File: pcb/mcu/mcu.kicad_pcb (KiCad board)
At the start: 2 copper layers, 99 x 34 mm, 46 parts, among them J1 Conn_01x02_Male, J3 Conn_01x05_Female, P1 USB_C_6PIN_POWER, SW1 SW_BOOT, SW2 SW_Push_SPDT, U1 SPX3819M5-L-3-3, U2 LTC4054ES5-4.2, U3 LM358, U4 ESP-12S, U6 SGM3002_XMS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

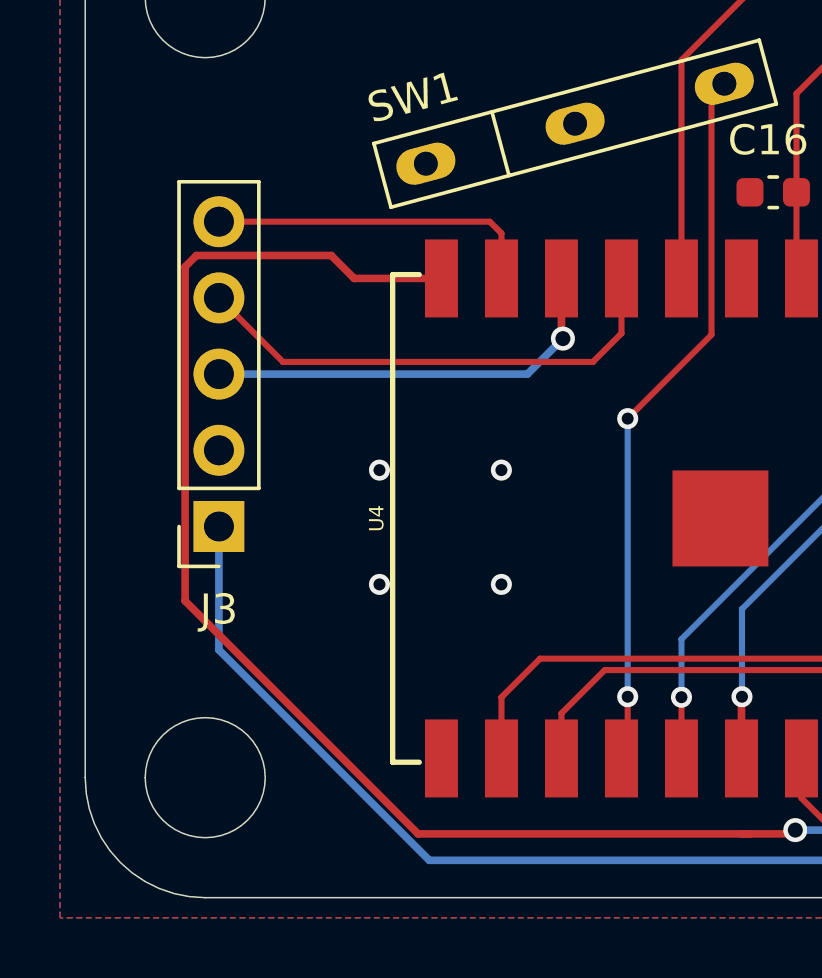
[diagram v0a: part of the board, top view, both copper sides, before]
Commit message: PCB调整 3D装配图
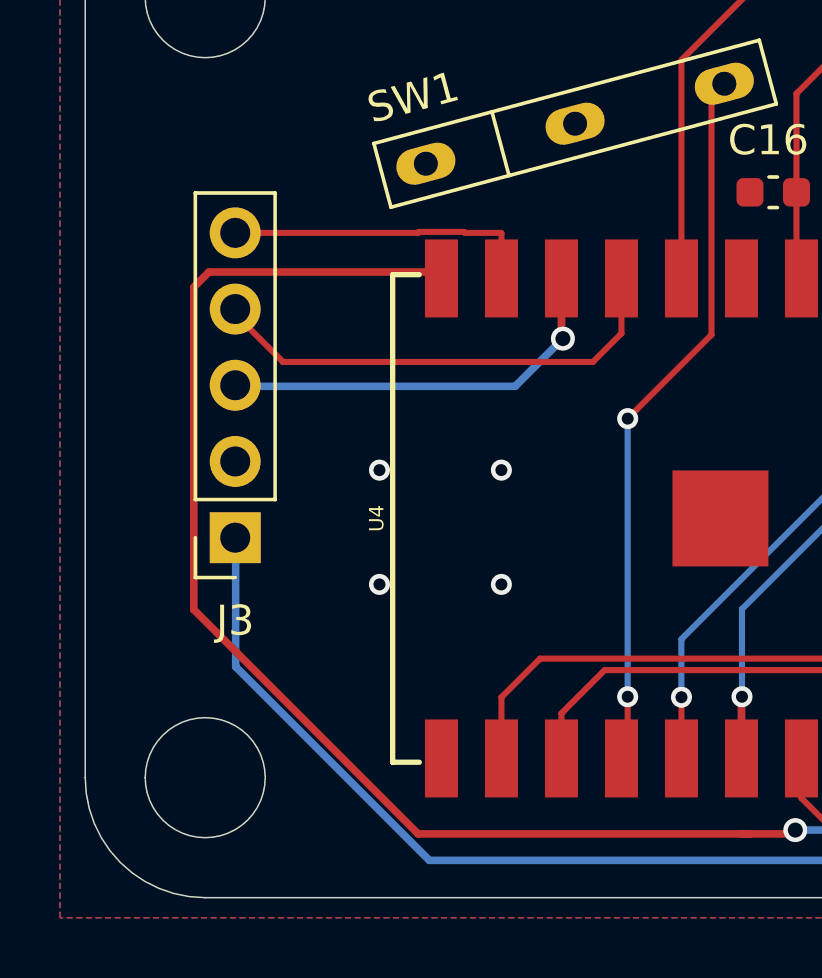
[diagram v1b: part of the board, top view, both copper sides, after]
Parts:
- moved J3 0.66 mm to (36.3, 89.7)
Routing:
- net +3V3: track 143.8 -> 142.5 mm
